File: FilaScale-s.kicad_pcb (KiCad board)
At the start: 2 copper layers, 50 x 50 mm, 10 parts, among them J1 HX711MOD, J2 Arduino_Nano_v3.x, J3 BME-280, J4 RFID, M3 MountingHole_3.2mm_M3_ISO7380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

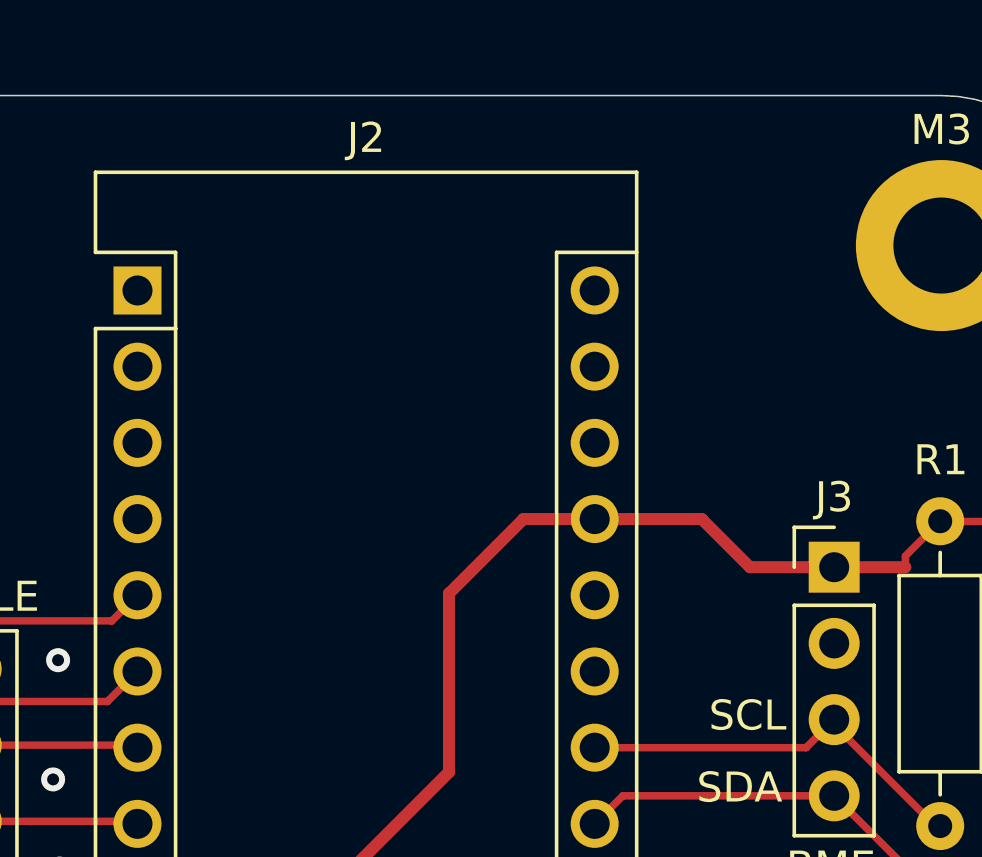
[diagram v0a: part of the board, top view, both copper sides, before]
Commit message: Rounded the corners, made it 50x50mm in size Added a couple of entries to .gitignore
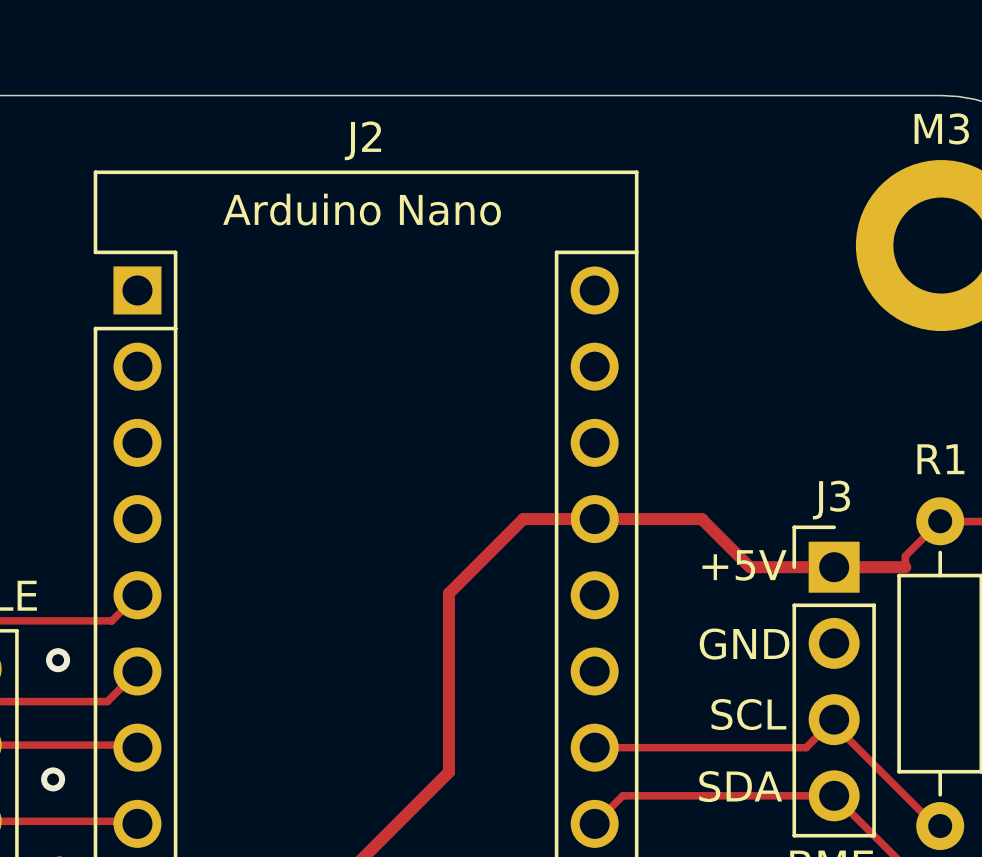
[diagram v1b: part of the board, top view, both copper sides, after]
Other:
- board text added: "Arduino Nano"

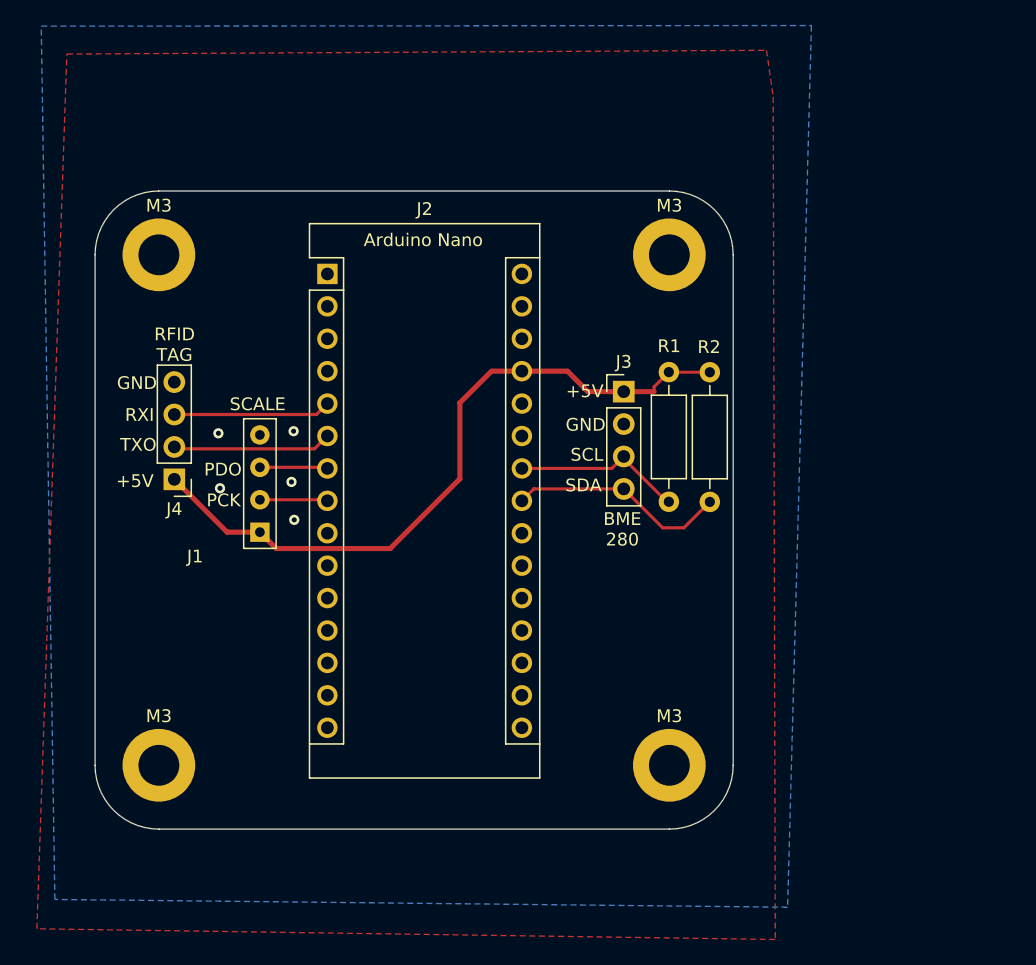
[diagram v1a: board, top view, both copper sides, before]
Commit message: Add expansion connectors for things I can't forsee but users might want available
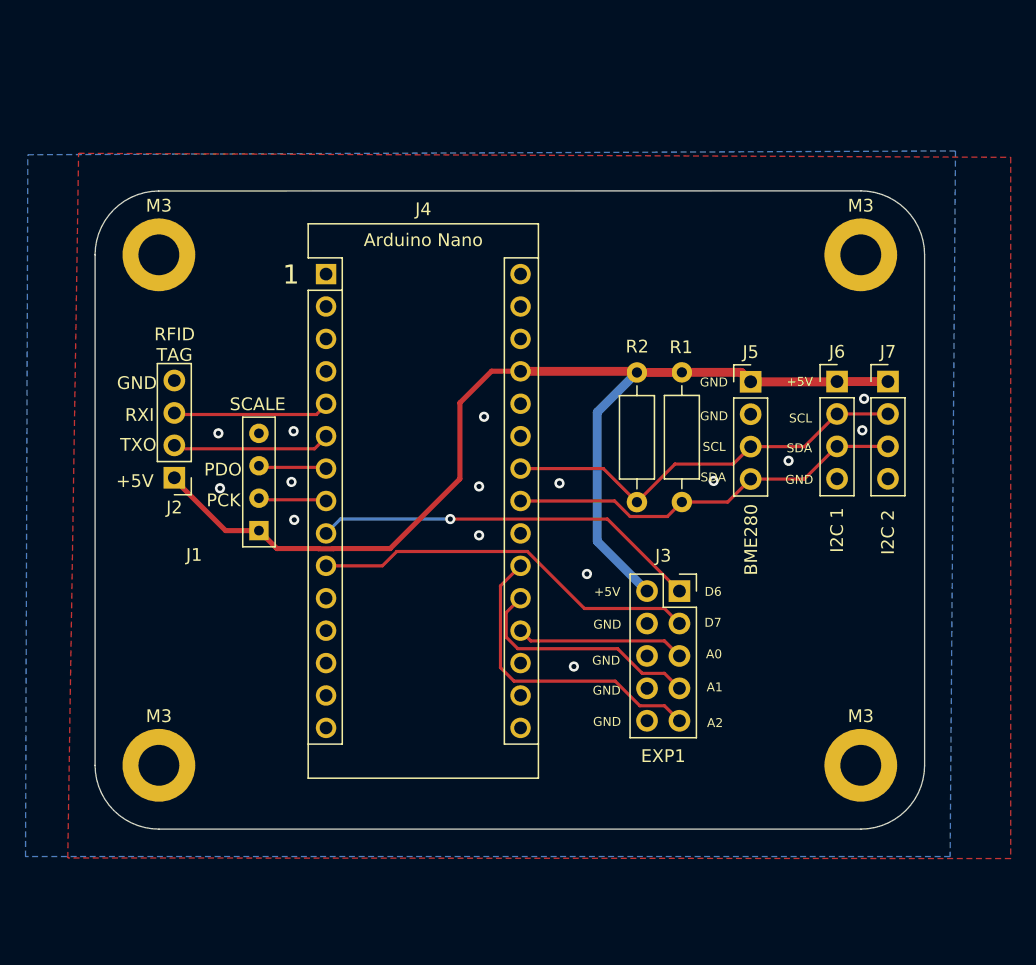
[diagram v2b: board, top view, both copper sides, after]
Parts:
- removed the M3 at (83.0, 168.0)
- removed the M3 at (83.0, 128.0)
- added J5: BME280, Connector_PinHeader_2.54mm:PinHeader_1x04_P2.54mm_Vertical, F.Cu at (89.4, 137.9)
- added J6: I2C 1, Connector_PinHeader_2.54mm:PinHeader_1x04_P2.54mm_Vertical, F.Cu at (96.1, 137.9)
- added J7: I2C 2, Connector_PinHeader_2.54mm:PinHeader_1x04_P2.54mm_Vertical, F.Cu at (100.1, 137.9)
- added M3: MountingHole_3.2mm_M3_ISO7380_Pad, MountingHole:MountingHole_3.2mm_M3_ISO7380_Pad, F.Cu at (98.0, 168.0)
- added M3: MountingHole_3.2mm_M3_ISO7380_Pad, MountingHole:MountingHole_3.2mm_M3_ISO7380_Pad, F.Cu at (98.0, 128.0)
- J2: value Arduino_Nano_v3.x -> RFID; footprint Module:Arduino_Nano -> Connector_PinHeader_2.54mm:PinHeader_1x04_P2.54mm_Vertical
- J3: value BME-280 -> EXP1; footprint Connector_PinHeader_2.54mm:PinHeader_1x04_P2.54mm_Vertical -> Connector_PinSocket_2.54mm:PinSocket_2x05_P2.54mm_Vertical
- J4: value RFID -> Arduino_Nano_v3.x; footprint Connector_PinHeader_2.54mm:PinHeader_1x04_P2.54mm_Vertical -> Module:Arduino_Nano
- moved J4 20.0 mm to (56.1, 129.5), turned to 0 degrees
- moved J2 20.0 mm to (44.2, 145.5), turned to 180 degrees
- moved J3 16.2 mm to (83.8, 154.3)
- moved R2 2.50 mm to (80.5, 147.4)
- moved R1 2.19 mm to (84.0, 137.2)
- moved J1 0.14 mm to (50.8, 149.6)
- renumbered R2 to R1, R1 to R2
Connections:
- J2 pad 1: Net-(J2-Pad1) -> +5V
- J2 pad 2: Net-(J2-Pad2) -> /RFID_TXO
- J2 pad 3: Net-(J2-Pad3) -> /RFID_RXI
- J3 pad 1: +5V -> /D6
- J3 pad 2: GND -> +5V
- J3 pad 3: /SCL -> /D7
- J3 pad 4: /SDA -> GND
- J4 pad 1: +5V -> Net-(J4-Pad1)
- J4 pad 2: /RFID_TXO -> Net-(J4-Pad2)
- J4 pad 3: /RFID_RXI -> Net-(J4-Pad3)
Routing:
- net +5V: track 55.0 -> 88.0 mm
- net /D6: track 0.00 -> 30.5 mm, vias 0 -> 1
- net /D7: track 0.00 -> 30.5 mm
- net /A2: track 0.00 -> 24.4 mm
- net /SCL: track 13.5 -> 32.8 mm
- net /A1: track 0.00 -> 18.7 mm
- net /SDA: track 17.2 -> 31.6 mm
- net /A0: track 0.00 -> 13.3 mm
- net GND: vias 5 -> 15
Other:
- board size 50 x 50 mm -> 65 x 50 mm
- board text added: "1"
- board text added: "A0"
- board text added: "A1"
- board text added: "A2"
- board text added: "D6"
- board text added: "D7"
- board text removed: "BME 280"

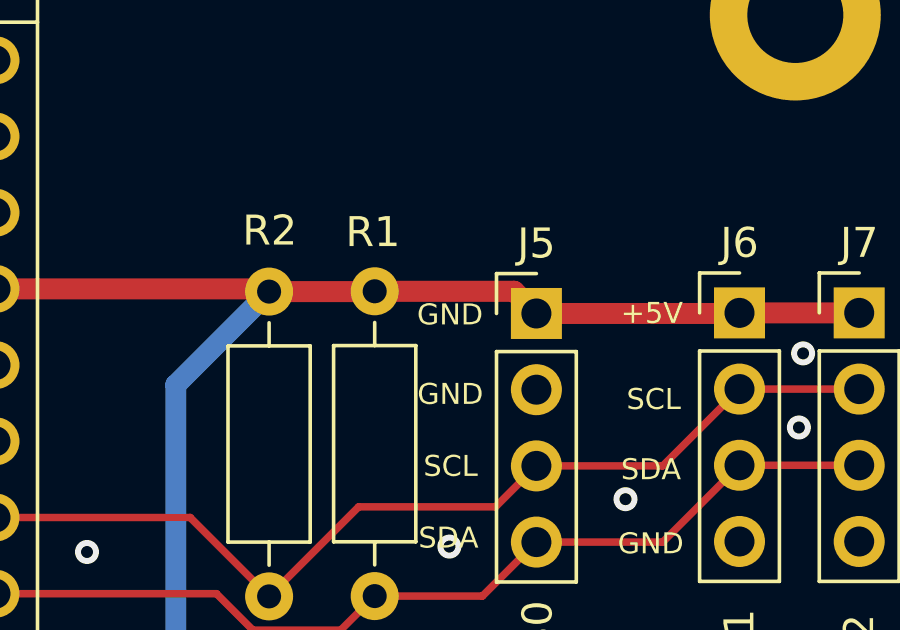
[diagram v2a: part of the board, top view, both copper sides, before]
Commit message: Fix label on front silkscreen;
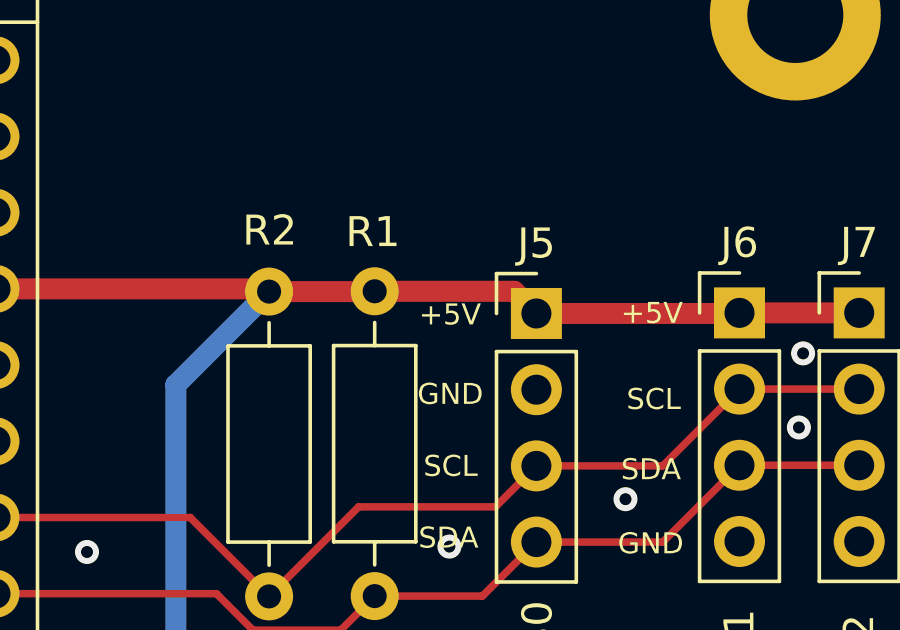
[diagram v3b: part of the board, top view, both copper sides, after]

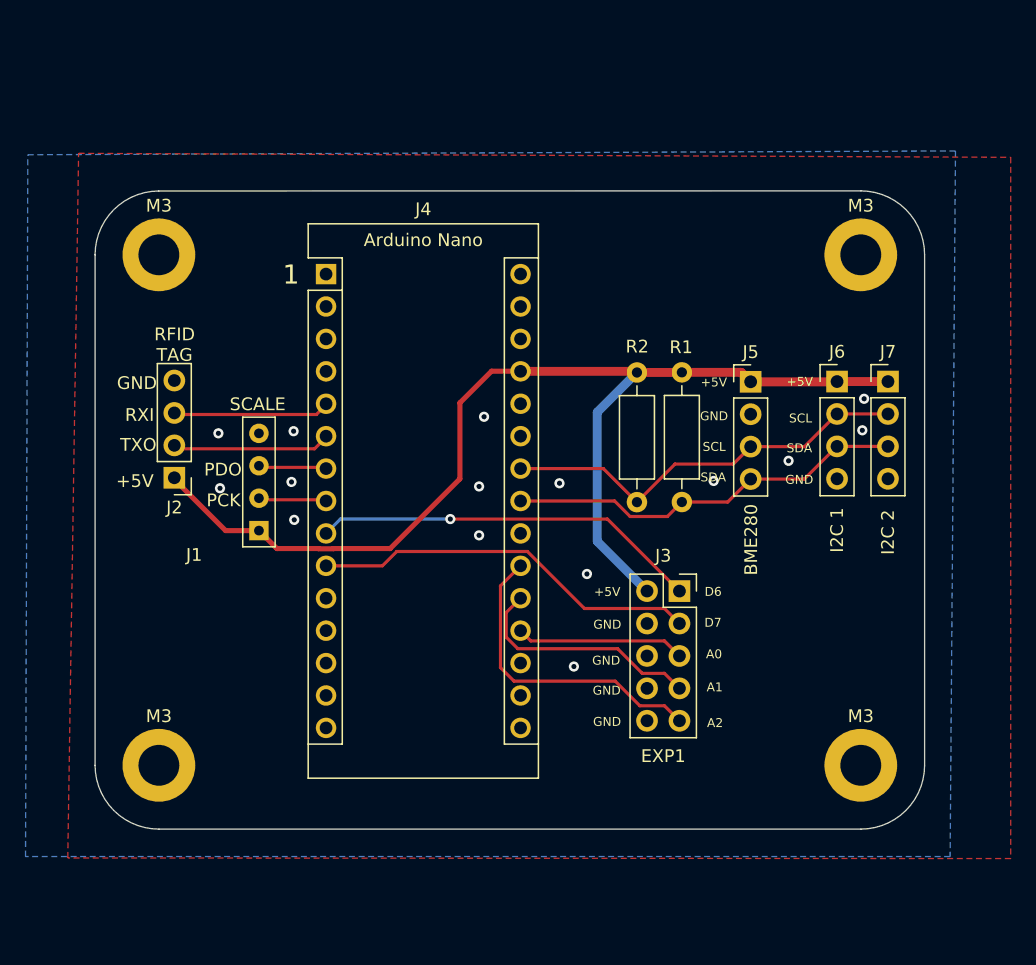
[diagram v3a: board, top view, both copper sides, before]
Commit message: Cleanup, add bypass and decoupling caps, add expansion port
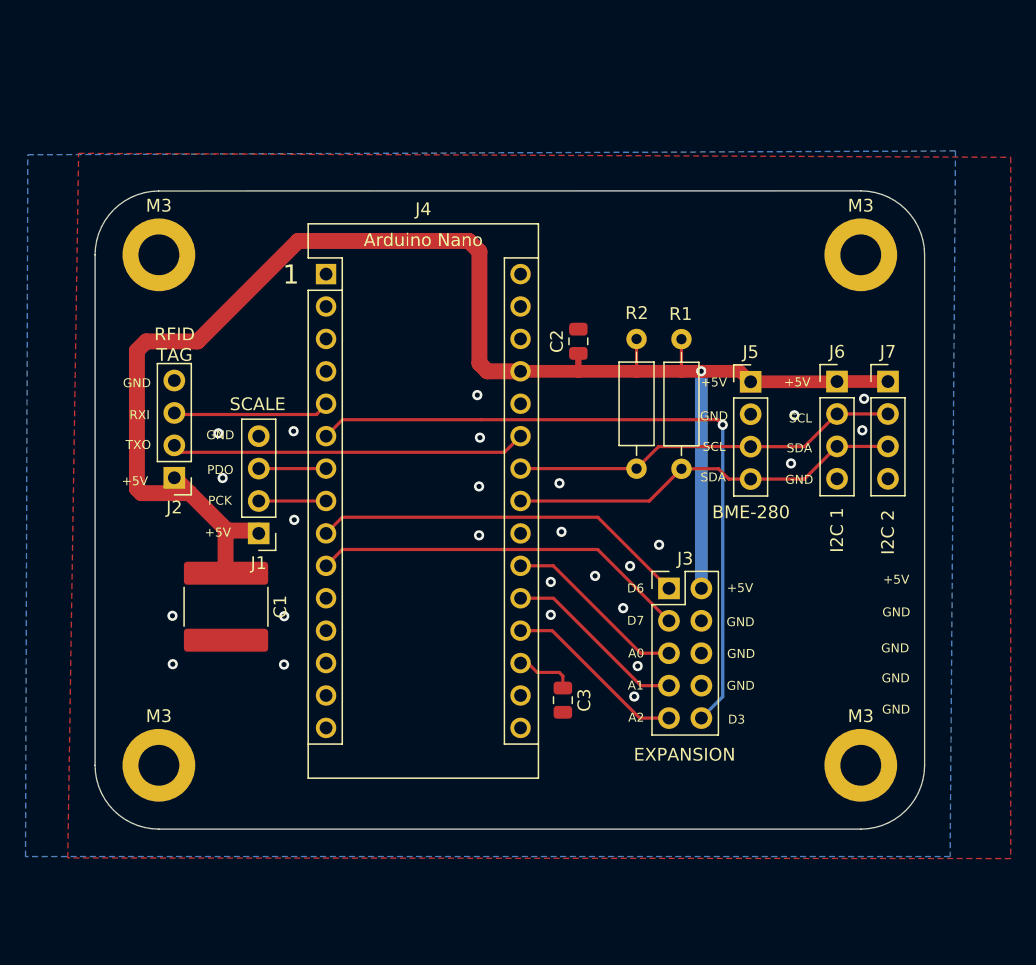
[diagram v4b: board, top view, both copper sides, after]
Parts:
- added C1: 10uF, Capacitor_SMD:C_2225_5664Metric_Pad1.80x6.60mm_HandSolder, F.Cu at (48.3, 155.6)
- added C2: .1uF, Capacitor_SMD:C_0805_2012Metric, F.Cu at (75.9, 134.8)
- added C3: .1uF, Capacitor_SMD:C_0805_2012Metric, F.Cu at (74.7, 162.9)
- J1: footprint HX711MOD_F -> Connector_PinHeader_2.54mm:PinHeader_1x04_P2.54mm_Vertical
- J3: footprint Connector_PinSocket_2.54mm:PinSocket_2x05_P2.54mm_Vertical -> Connector_PinHeader_2.54mm:PinHeader_2x05_P2.54mm_Vertical
- J5: value BME280 -> BME-280
- moved R2 2.63 mm to (80.4, 144.8)
- moved R1 2.60 mm to (83.9, 134.6)
- moved J3 0.85 mm to (83.0, 154.1)
- moved J1 0.22 mm to (50.8, 149.8)
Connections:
- J3 pad 10: GND -> /D3
- J3 pad 5: /A0 -> /A2
- J3 pad 9: /A2 -> /A0
- J4 pad 18: Net-(J4-Pad18) -> /AREF
- J4 pad 25: Net-(J4-Pad25) -> /RFID_TXO
- J4 pad 6: /RFID_TXO -> /D3
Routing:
- net /D3: track 0.00 -> 55.5 mm, vias 0 -> 1
- net +5V: track 88.0 -> 122.7 mm, vias 0 -> 1
- net /RFID_TXO: track 12.5 -> 27.8 mm
- net /A2: track 24.4 -> 14.5 mm
- net /AREF: track 0.00 -> 4.67 mm
- net /A1: track 18.7 -> 14.5 mm
- net /SCL: track 32.8 -> 30.6 mm
- net /A0: track 13.3 -> 14.5 mm
- net /D6: track 30.5 -> 29.7 mm, vias 1 -> 0
- net /D7: track 30.5 -> 29.7 mm
- net GND: vias 15 -> 26
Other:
- board text added: "D3"
- board text added: "EXPANSION"
- board text added: "FilaScale-S"
- board text added: "rev 2"

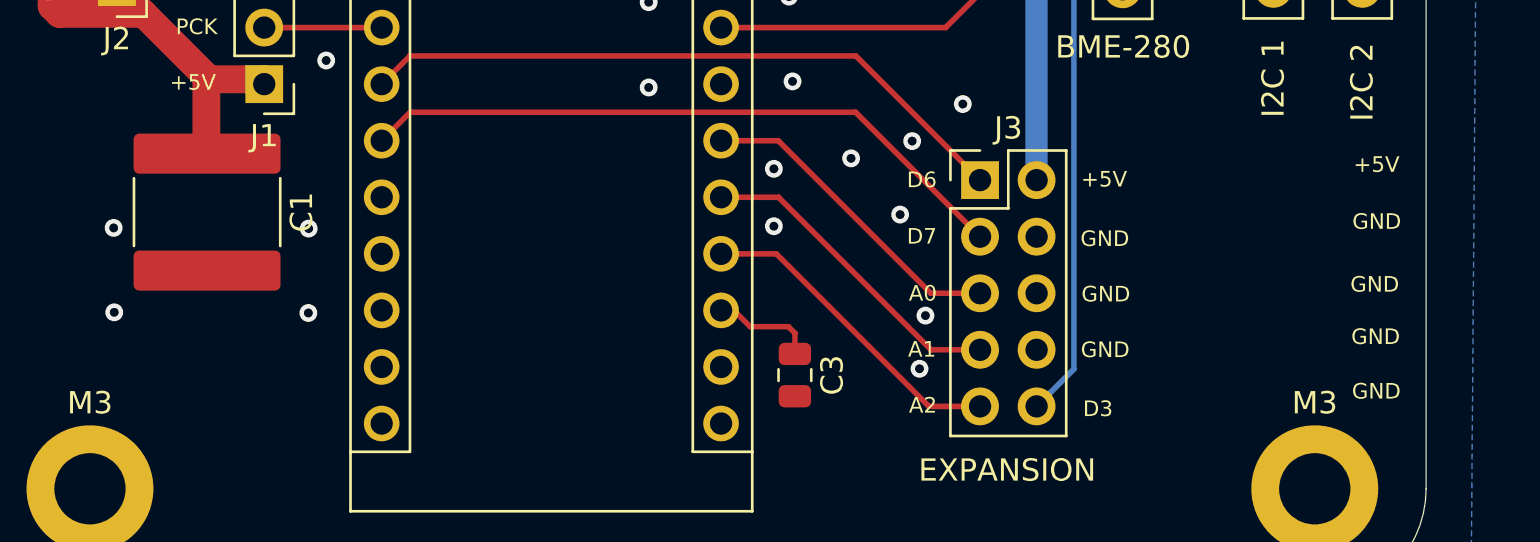
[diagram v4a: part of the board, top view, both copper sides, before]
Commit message: Fix silkscreen
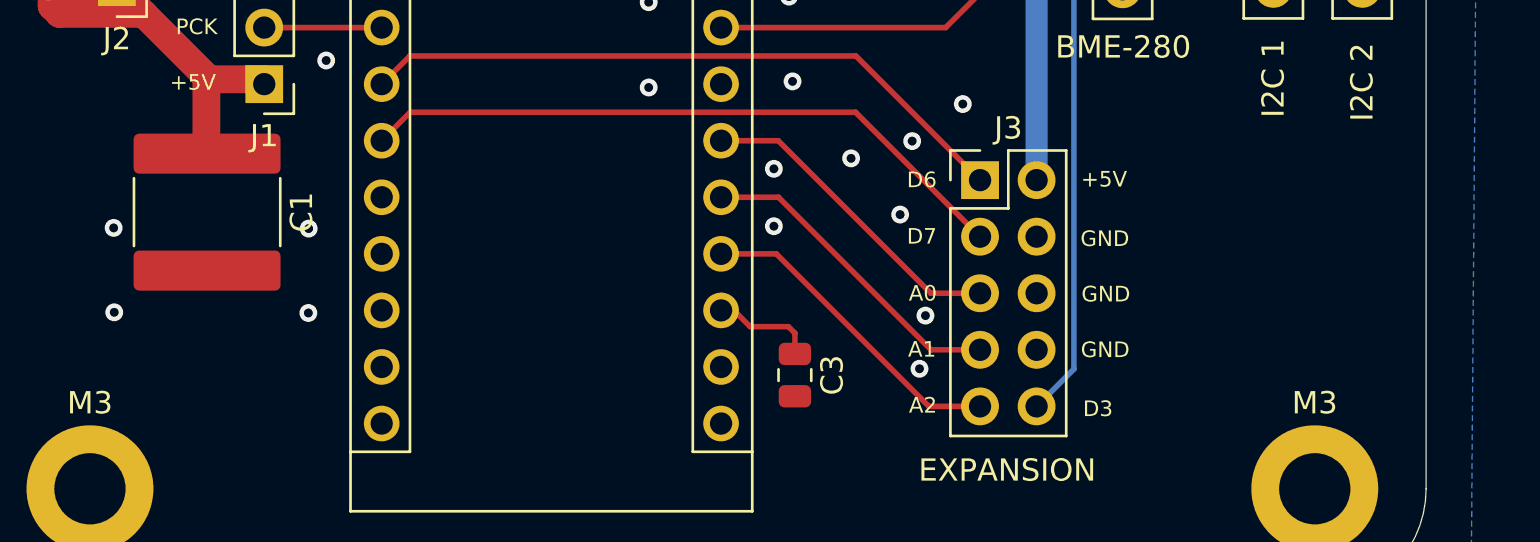
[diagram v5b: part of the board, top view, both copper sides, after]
